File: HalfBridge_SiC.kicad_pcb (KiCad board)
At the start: 2 copper layers, 100 x 100 mm, 19 parts, among them Q1 C3M0075120J, Q2 C3M0075120J, U1 UCC21520ADW, U2 TBA2-0522, U3 TBA2-0522

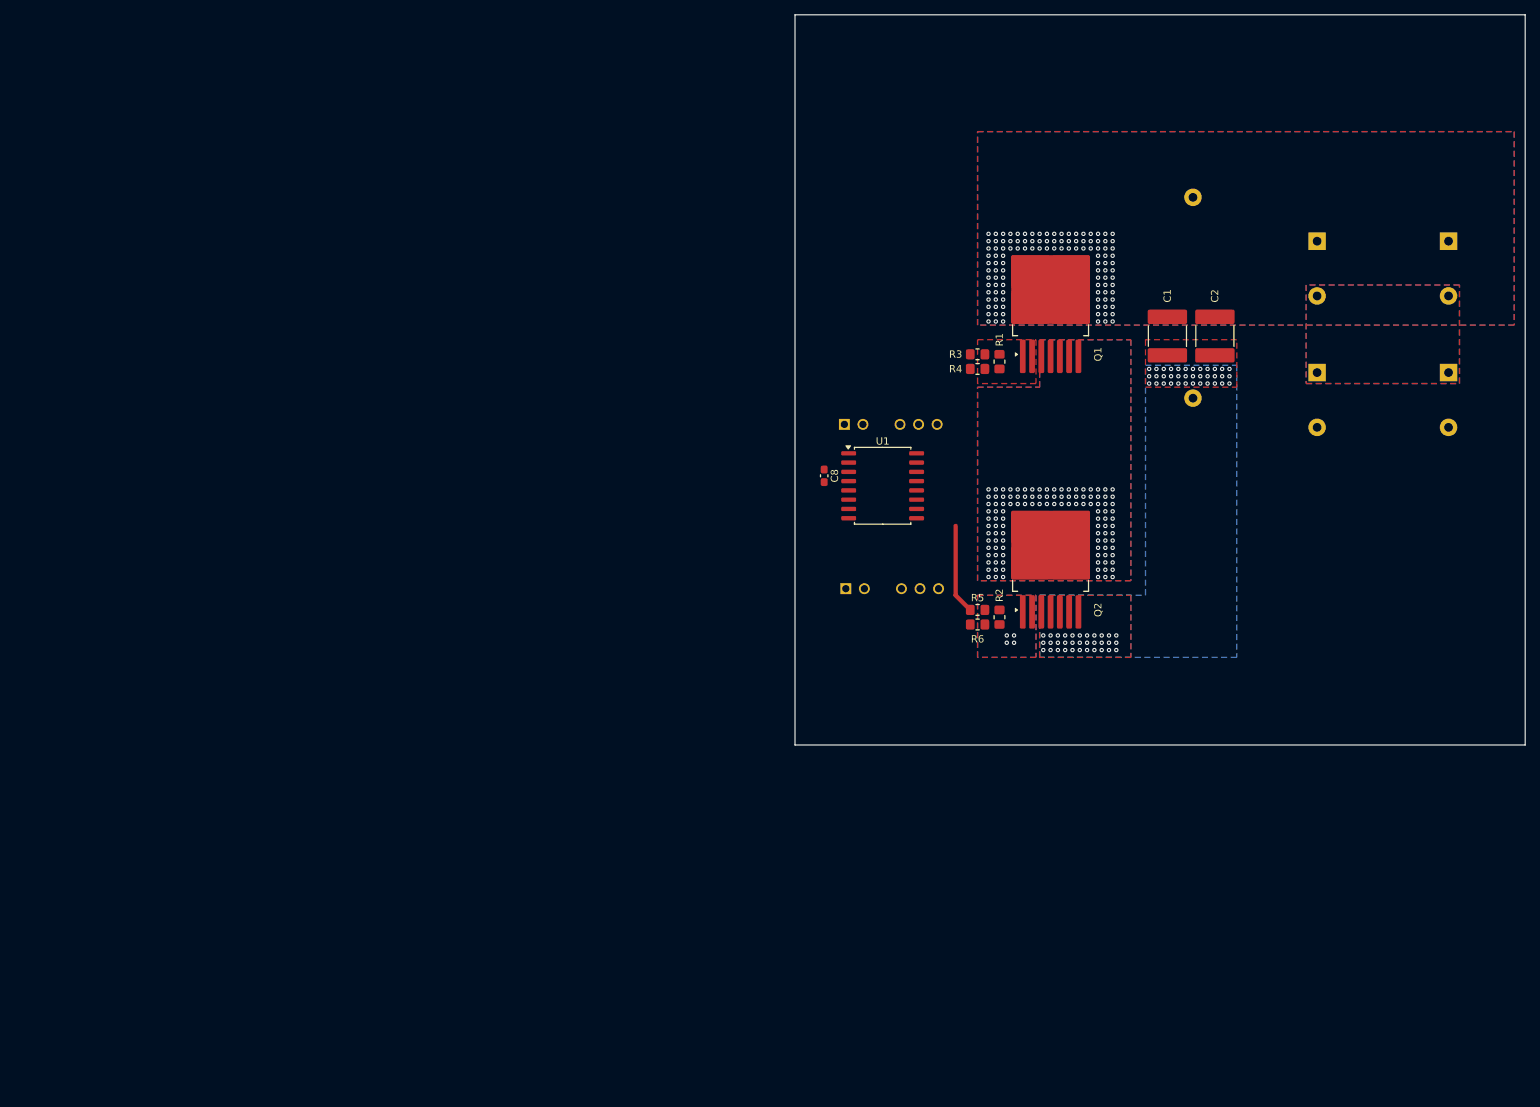
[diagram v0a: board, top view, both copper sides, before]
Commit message: gate driver
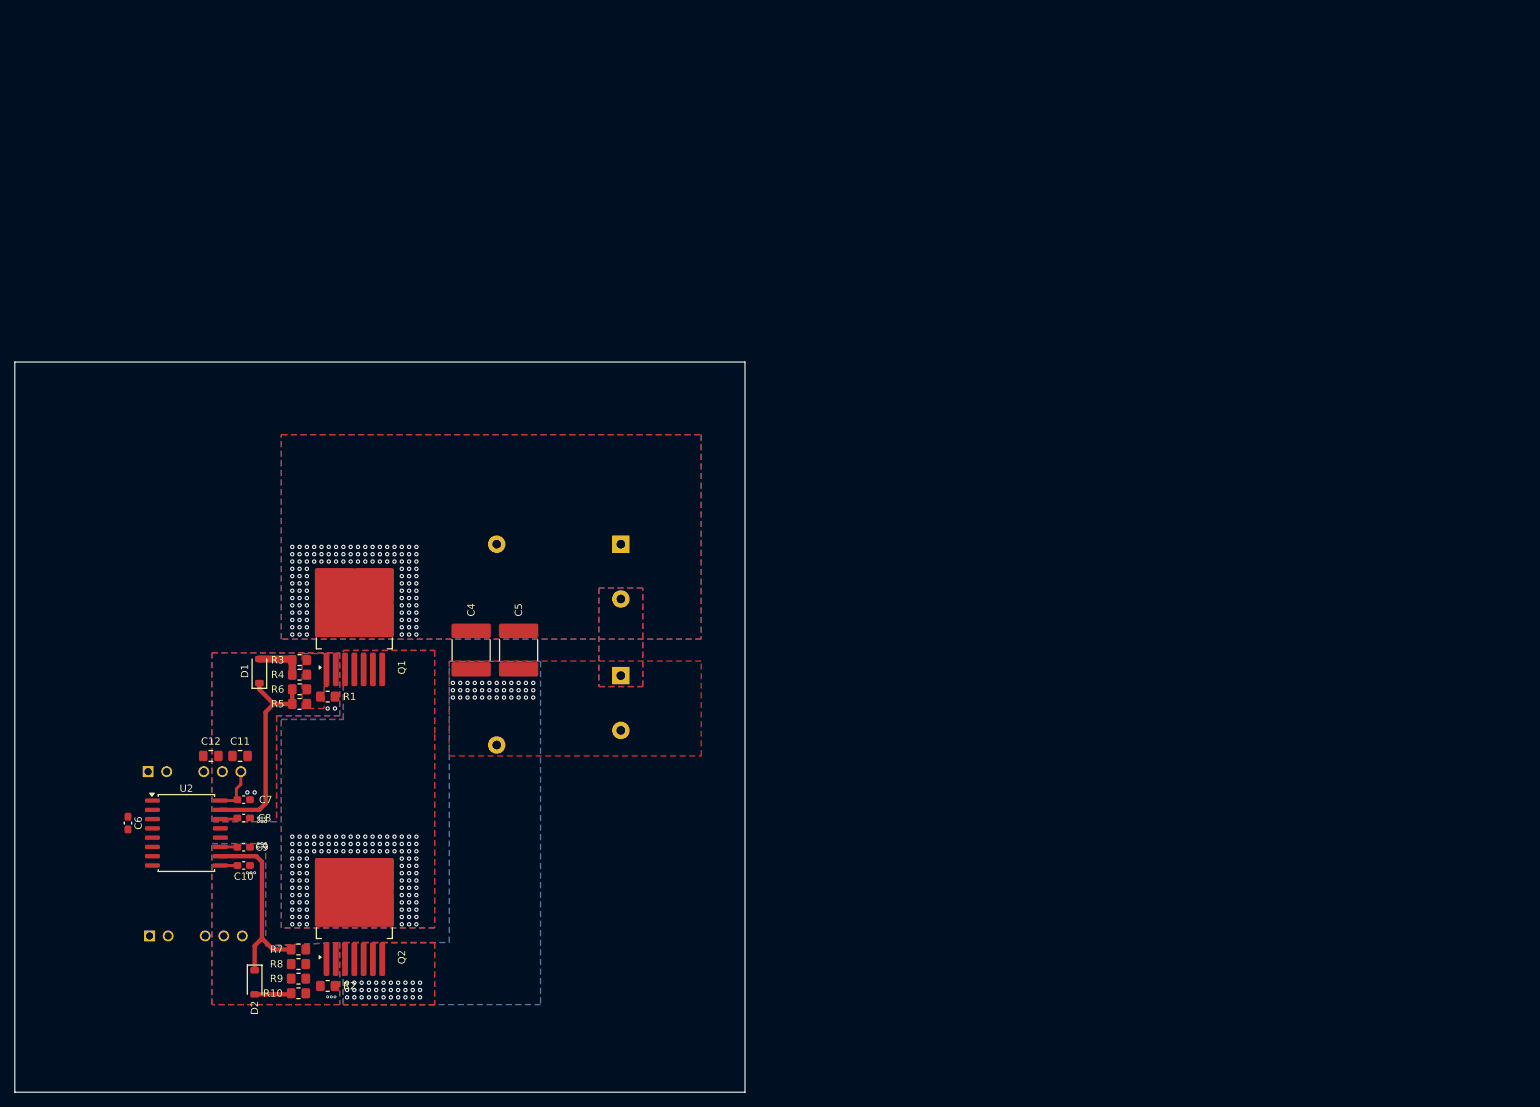
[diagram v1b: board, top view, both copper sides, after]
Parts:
- removed the C6 at (231.5, 63.5)
- added C10: C, Capacitor_SMD:C_0603_1608Metric_Pad1.08x0.95mm_HandSolder, F.Cu at (66.5, 149.0)
- added C11: C, Capacitor_SMD:C_0805_2012Metric_Pad1.18x1.45mm_HandSolder, F.Cu at (66.0, 134.0)
- added C12: C, Capacitor_SMD:C_0805_2012Metric_Pad1.18x1.45mm_HandSolder, F.Cu at (62.0, 134.0)
- added C8: 100n, Capacitor_SMD:C_0603_1608Metric_Pad1.08x0.95mm_HandSolder, F.Cu at (66.5, 142.5)
- added C9: C, Capacitor_SMD:C_0603_1608Metric_Pad1.08x0.95mm_HandSolder, F.Cu at (66.5, 146.5)
- added D1: D_Schottky, Diode_SMD:D_SOD-123, F.Cu at (68.7, 122.4)
- added D2: D_Schottky, Diode_SMD:D_SOD-123, F.Cu at (68.0, 165.0)
- added R10: R, Resistor_SMD:R_0805_2012Metric_Pad1.20x1.40mm_HandSolder, F.Cu at (74.0, 166.5)
- added R3: R, Resistor_SMD:R_0805_2012Metric_Pad1.20x1.40mm_HandSolder, F.Cu at (74.2, 120.9)
- added R5: R, Resistor_SMD:R_0805_2012Metric_Pad1.20x1.40mm_HandSolder, F.Cu at (74.2, 126.9)
- added R9: R, Resistor_SMD:R_0805_2012Metric_Pad1.20x1.40mm_HandSolder, F.Cu at (74.0, 164.5)
- C7: value C -> 100n; footprint Capacitor_THT:CP_Radial_D17.0mm_P7.50mm -> Capacitor_SMD:C_0603_1608Metric_Pad1.08x0.95mm_HandSolder; moved to F.Cu
- moved C7 175.1 mm to (66.5, 140.0), turned to 0 degrees
- moved U3 106.6 mm to (53.6, 158.6)
- moved C6 106.6 mm to (50.6, 143.2)
- moved Q2 106.6 mm to (81.7, 154.2)
- moved U1 106.6 mm to (53.4, 136.1)
- moved U2 106.6 mm to (58.6, 144.6)
- moved C3 106.5 mm to (101.2, 105.0)
- moved R2 104.9 mm to (78.0, 165.5), turned to 0 degrees
- moved C4 104.6 mm to (97.7, 119.5)
- moved C5 104.6 mm to (104.2, 119.5)
- moved Q1 104.5 mm to (81.7, 114.5)
- moved C1 104.0 mm to (118.2, 105.0)
- moved C2 104.0 mm to (118.2, 123.0)
- moved R7 104.0 mm to (74.0, 160.5)
- moved R8 104.0 mm to (74.0, 162.5)
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- renumbered C4 to C1, C5 to C2, C1 to C4, C2 to C5, C8 to C6, R3 to R6, R5 to R7, R6 to R8, U2 to U1, U1 to U2
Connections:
- C7 pad 1: /HalfBridge_Power/dcm -> /HalfBridge_GateDriver/vddh
- C7 pad 2: /HalfBridge_Power/dcn -> /HalfBridge_GateDriver/kh
- R4 pad 1: /HalfBridge_GateDriver/gonh -> /HalfBridge_GateDriver/asgh
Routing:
- net /HalfBridge_GateDriver/gonh: track 0.00 -> 28.8 mm
- net /HalfBridge_GateDriver/gonl: track 12.3 -> 25.9 mm
- net /HalfBridge_GateDriver/vddh: track 0.00 -> 6.61 mm
- net /HalfBridge_GateDriver/asgh: track 0.00 -> 6.56 mm
- net /HalfBridge_GateDriver/asgl: track 0.00 -> 5.06 mm
- net /HalfBridge_GateDriver/vssh: track 0.00 -> 2.40 mm
- net /HalfBridge_GateDriver/vddl: track 0.00 -> 2.35 mm
- net /HalfBridge_GateDriver/vssl: track 0.00 -> 2.34 mm
- net /HalfBridge_GateDriver/kl: vias 4 -> 12
- net /HalfBridge_GateDriver/kh: vias 0 -> 10
- added copper zone on B.Cu, net /HalfBridge_GateDriver/kh
- added copper zone on F.Cu, net /HalfBridge_Power/gh

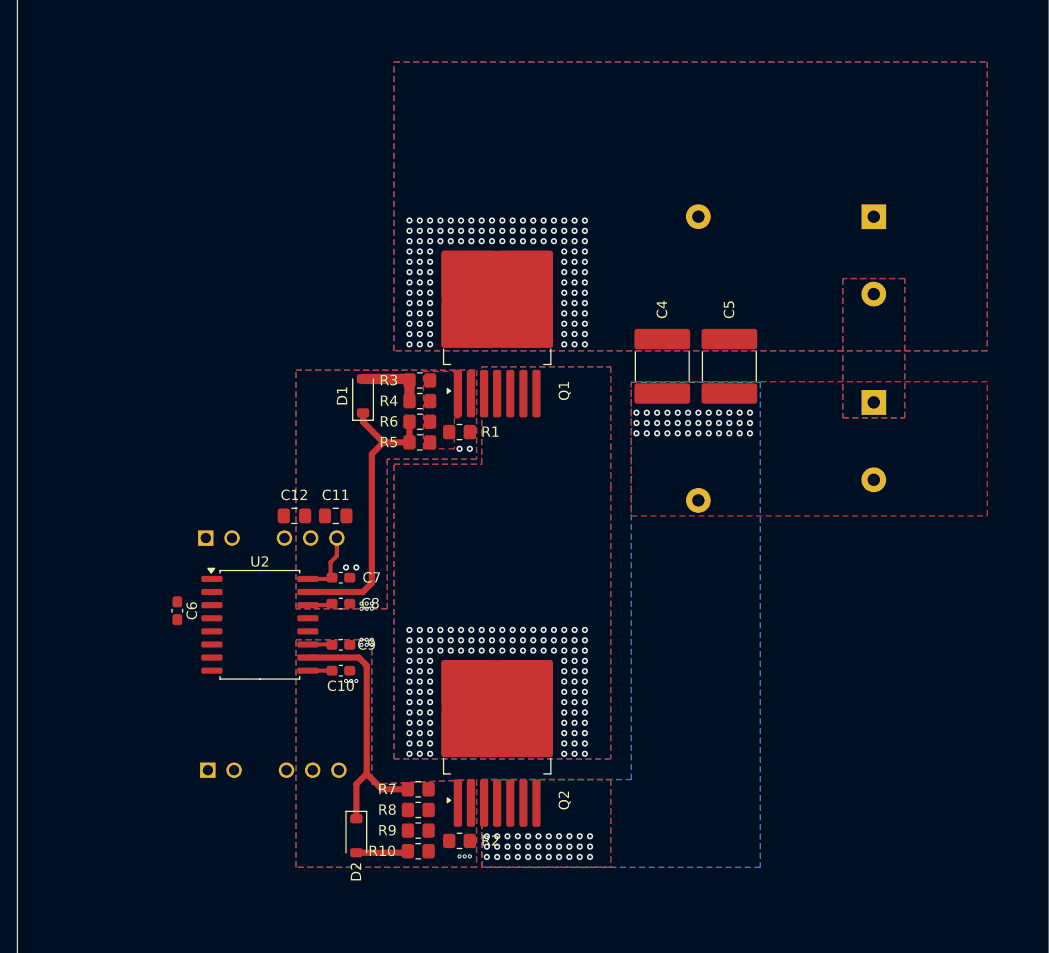
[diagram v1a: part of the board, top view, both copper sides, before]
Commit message: symbol library gatedriver
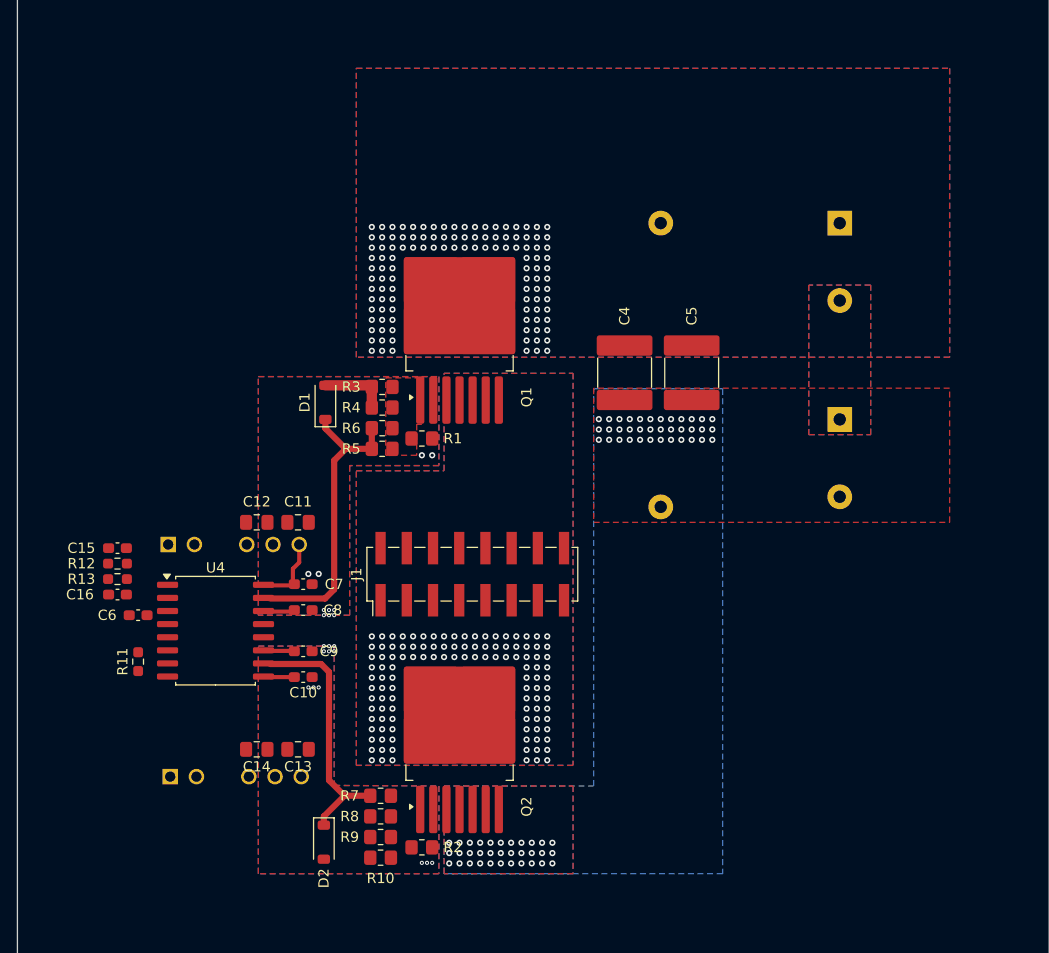
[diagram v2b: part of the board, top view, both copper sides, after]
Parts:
- removed U2: UCC21520ADW, Package_SO:SOIC-16W_7.5x10.3mm_P1.27mm
- added C13: C, Capacitor_SMD:C_0805_2012Metric_Pad1.18x1.45mm_HandSolder, F.Cu at (62.4, 156.6)
- added C14: C, Capacitor_SMD:C_0805_2012Metric_Pad1.18x1.45mm_HandSolder, F.Cu at (58.4, 156.6)
- added C15: C, Capacitor_SMD:C_0603_1608Metric_Pad1.08x0.95mm_HandSolder, F.Cu at (44.9, 137.1)
- added C16: C, Capacitor_SMD:C_0603_1608Metric_Pad1.08x0.95mm_HandSolder, F.Cu at (44.9, 141.6)
- added J1: Conn_02x08_Odd_Even, Connector_PinHeader_2.54mm:PinHeader_2x08_P2.54mm_Vertical_SMD, F.Cu at (79.2, 139.7)
- added R11: R, Resistor_SMD:R_0603_1608Metric_Pad0.98x0.95mm_HandSolder, F.Cu at (46.9, 148.1)
- added R12: R, Resistor_SMD:R_0603_1608Metric_Pad0.98x0.95mm_HandSolder, F.Cu at (44.9, 138.6)
- added R13: R, Resistor_SMD:R_0603_1608Metric_Pad0.98x0.95mm_HandSolder, F.Cu at (44.9, 140.1)
- added U4: NCD57252, Package_SO:SOIC-16W_7.5x10.3mm_P1.27mm, F.Cu at (54.4, 145.1)
- C1, C2: footprint Capacitor_THT:CP_Radial_D17.0mm_P7.50mm -> Capacitor_THT:CP_Radial_D18.0mm_P7.50mm
- moved C6 3.82 mm to (46.9, 143.6), turned to 180 degrees
- moved C3 3.70 mm to (97.5, 105.6)
- moved C4 3.70 mm to (94.0, 120.1)
- moved C5 3.70 mm to (100.5, 120.1)
- moved D1 3.70 mm to (65.0, 123.0)
- moved Q1 3.70 mm to (78.0, 115.1)
- moved Q2 3.70 mm to (78.0, 154.8)
- moved R1 3.70 mm to (74.3, 126.5)
- moved R10 3.70 mm to (70.3, 167.1)
- moved R2 3.70 mm to (74.3, 166.1)
- moved R3 3.70 mm to (70.5, 121.5)
- moved R4 3.70 mm to (70.5, 123.5)
- moved R5 3.70 mm to (70.5, 127.5)
- moved R6 3.70 mm to (70.5, 125.5)
- moved R7 3.70 mm to (70.3, 161.1)
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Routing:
- net /HalfBridge_GateDriver/asgl: track 5.06 -> 0.21 mm
- net /HalfBridge_GateDriver/gonl: track 25.9 -> 24.8 mm
